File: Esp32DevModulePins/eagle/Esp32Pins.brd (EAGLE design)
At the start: 100 x 80 mm, 2 parts

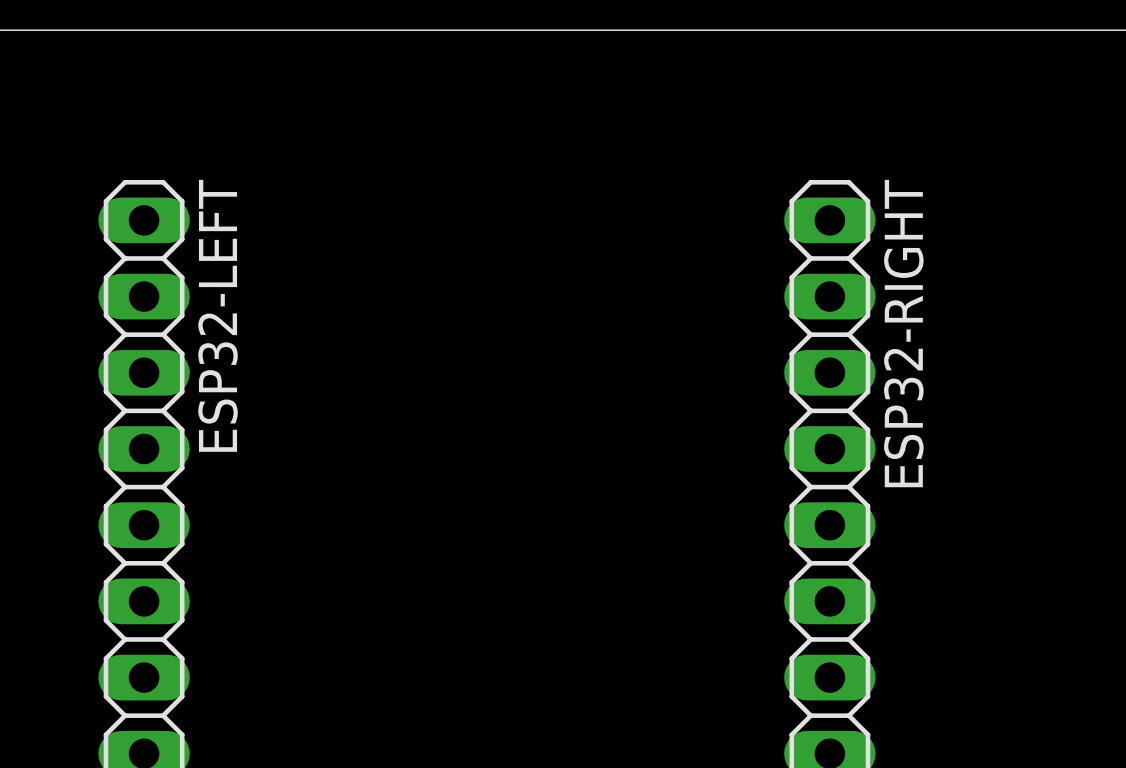
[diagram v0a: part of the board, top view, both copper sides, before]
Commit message: Corrected left vs right nomenclature
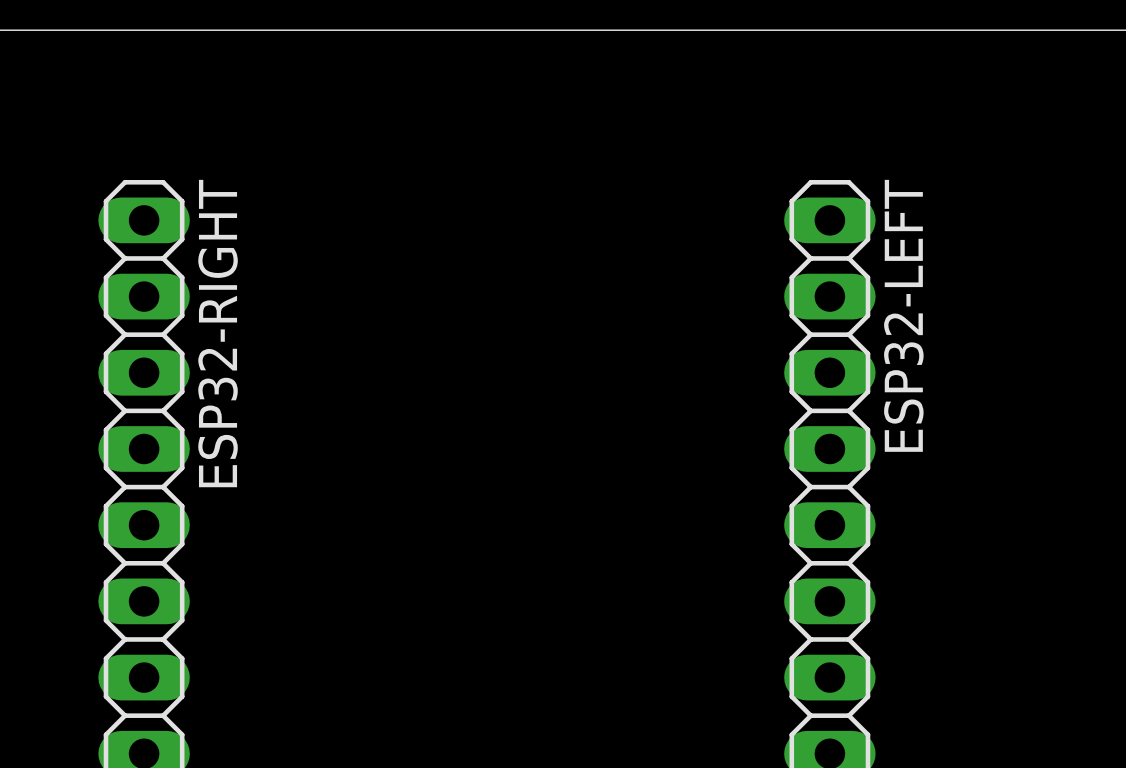
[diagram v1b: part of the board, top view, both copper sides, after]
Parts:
- moved ESP32-LEFT 22.9 mm to (29.2, 55.9)
- moved ESP32-RIGHT 22.9 mm to (6.35, 55.9)
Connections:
- net 3V3: now also ESP32-RIGHT.1; no longer ESP32-LEFT.1
- net D12: now also ESP32-LEFT.4; no longer ESP32-RIGHT.4
- net D13: now also ESP32-LEFT.3; no longer ESP32-RIGHT.3
- net D14: now also ESP32-LEFT.5; no longer ESP32-RIGHT.5
- net D15: now also ESP32-RIGHT.3; no longer ESP32-LEFT.3
- net D16: now also ESP32-RIGHT.6; no longer ESP32-LEFT.6
- net D17: now also ESP32-RIGHT.7; no longer ESP32-LEFT.7
- net D18: now also ESP32-RIGHT.9; no longer ESP32-LEFT.9
- net D19: now also ESP32-RIGHT.10; no longer ESP32-LEFT.10
- net D1_TX: now also ESP32-RIGHT.13; no longer ESP32-LEFT.13
- net D2: now also ESP32-RIGHT.4; no longer ESP32-LEFT.4
- net D21: now also ESP32-RIGHT.11; no longer ESP32-LEFT.11
- net D22: now also ESP32-RIGHT.14; no longer ESP32-LEFT.14
- net D23: now also ESP32-RIGHT.15; no longer ESP32-LEFT.15
- net D25: now also ESP32-LEFT.8; no longer ESP32-RIGHT.8
- net D26: now also ESP32-LEFT.7; no longer ESP32-RIGHT.7
- net D27: now also ESP32-LEFT.6; no longer ESP32-RIGHT.6
- net D32: now also ESP32-LEFT.10; no longer ESP32-RIGHT.10
- net D33: now also ESP32-LEFT.9; no longer ESP32-RIGHT.9
- net D3_RX: now also ESP32-RIGHT.12; no longer ESP32-LEFT.12
- net D4: now also ESP32-RIGHT.5; no longer ESP32-LEFT.5
- net D5: now also ESP32-RIGHT.8; no longer ESP32-LEFT.8
- net I34: now also ESP32-LEFT.12; no longer ESP32-RIGHT.12
- net I35: now also ESP32-LEFT.11; no longer ESP32-RIGHT.11
- net I36: now also ESP32-LEFT.14; no longer ESP32-RIGHT.14
- net I39: now also ESP32-LEFT.13; no longer ESP32-RIGHT.13
- net RESET: now also ESP32-LEFT.15; no longer ESP32-RIGHT.15
- net VIN: now also ESP32-LEFT.1; no longer ESP32-RIGHT.1
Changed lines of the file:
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@@
 <?xml version="1.0" encoding="utf-8"?>
 <!DOCTYPE eagle SYSTEM "eagle.dtd">
-<eagle version="9.5.2">
+<eagle version="9.6.2">
 <drawing>
 <settings>
@@
 </autorouter>
 <elements>
-<element name="ESP32-LEFT" library="pinhead" library_urn="urn:adsk.eagle:library:325" package="1X15" package3d_urn="urn:adsk.eagle:package:22424/2" value="0" x="6.35" y="55.88" smashed="yes" rot="R270">
+<element name="ESP32-RIGHT" library="pinhead" library_urn="urn:adsk.eagle:library:325" package="1X15" package3d_urn="urn:adsk.eagle:package:22424/2" value="0" x="6.35" y="55.88" smashed="yes" rot="R270">
 <attribute name="NAME" x="8.1788" y="75.0062" size="1.27" layer="25" ratio="10" rot="R270"/>
 <attribute name="POPULARITY" value="4" x="6.35" y="55.88" size="1.778" layer="27" rot="R270" display="off"/>
 </element>
-<element name="ESP32-RIGHT" library="pinhead" library_urn="urn:adsk.eagle:library:325" package="1X15" package3d_urn="urn:adsk.eagle:package:22424/2" value="0" x="29.21" y="55.88" smashed="yes" rot="R270">
+<element name="ESP32-LEFT" library="pinhead" library_urn="urn:adsk.eagle:library:325" package="1X15" package3d_urn="urn:adsk.eagle:package:22424/2" value="0" x="29.21" y="55.88" smashed="yes" rot="R270">
 <attribute name="NAME" x="31.0388" y="75.0062" size="1.27" layer="25" ratio="10" rot="R270"/>
 <attribute name="POPULARITY" value="4" x="29.21" y="55.88" size="1.778" layer="27" rot="R270" display="off"/>
@@
 <signals>
 <signal name="VIN">
+<contactref element="ESP32-LEFT" pad="1"/>
+</signal>
+<signal name="GND">
+<contactref element="ESP32-RIGHT" pad="2"/>
+<contactref element="ESP32-LEFT" pad="2"/>
+<wire x1="29.21" y1="71.12" x2="6.35" y2="71.12" width="0" layer="19" extent="1-1"/>
+</signal>
+<signal name="D13">
+<contactref element="ESP32-LEFT" pad="3"/>
+</signal>
+<signal name="D12">
+<contactref element="ESP32-LEFT" pad="4"/>
+</signal>
+<signal name="D27">
+<contactref element="ESP32-LEFT" pad="6"/>
+</signal>
+<signal name="D26">
+<contactref element="ESP32-LEFT" pad="7"/>
+</signal>
+<signal name="D25">
+<contactref element="ESP32-LEFT" pad="8"/>
+</signal>
+<signal name="D33">
+<contactref element="ESP32-LEFT" pad="9"/>
+</signal>
+<signal name="D32">
+<contactref element="ESP32-LEFT" pad="10"/>
+</signal>
+<signal name="I35">
+<contactref element="ESP32-LEFT" pad="11"/>
+</signal>
+<signal name="I36">
+<contactref element="ESP32-LEFT" pad="14"/>
+</signal>
+<signal name="RESET">
+<contactref element="ESP32-LEFT" pad="15"/>
+</signal>
+<signal name="D14">
+<contactref element="ESP32-LEFT" pad="5"/>
+</signal>
+<signal name="I39">
+<contactref element="ESP32-LEFT" pad="13"/>
+</signal>
+<signal name="I34">
+<contactref element="ESP32-LEFT" pad="12"/>
+</signal>
+<signal name="3V3">
 <contactref element="ESP32-RIGHT" pad="1"/>
 </signal>
-<signal name="GND">
-<contactref element="ESP32-LEFT" pad="2"/>
-<contactref element="ESP32-RIGHT" pad="2"/>
-<wire x1="29.21" y1="71.12" x2="6.35" y2="71.12" width="0" layer="19" extent="1-1"/>
-</signal>
-<signal name="D13">
+<signal name="D15">
 <contactref element="ESP32-RIGHT" pad="3"/>
 </signal>
-<signal name="D12">
+<signal name="D2">
 <contactref element="ESP32-RIGHT" pad="4"/>
 </signal>
-<signal name="D27">
+<signal name="D4">
+<contactref element="ESP32-RIGHT" pad="5"/>
+</signal>
+<signal name="D16">
 <contactref element="ESP32-RIGHT" pad="6"/>
 </signal>
-<signal name="D26">
+<signal name="D17">
 <contactref element="ESP32-RIGHT" pad="7"/>
 </signal>
-<signal name="D25">
+<signal name="D5">
 <contactref element="ESP32-RIGHT" pad="8"/>
 </signal>
-<signal name="D33">
+<signal name="D18">
 <contactref element="ESP32-RIGHT" pad="9"/>
 </signal>
-<signal name="D32">
+<signal name="D19">
 <contactref element="ESP32-RIGHT" pad="10"/>
 </signal>
-<signal name="I35">
+<signal name="D21">
 <contactref element="ESP32-RIGHT" pad="11"/>
 </signal>
-<signal name="I36">
+<signal name="D22">
 <contactref element="ESP32-RIGHT" pad="14"/>
 </signal>
-<signal name="RESET">
+<signal name="D23">
 <contactref element="ESP32-RIGHT" pad="15"/>
 </signal>
-<signal name="D14">
-<contactref element="ESP32-RIGHT" pad="5"/>
-</signal>
-<signal name="I39">
+<signal name="D3_RX">
+<contactref element="ESP32-RIGHT" pad="12"/>
+</signal>
+<signal name="D1_TX">
 <contactref element="ESP32-RIGHT" pad="13"/>
 </signal>
-<signal name="I34">
-<contactref element="ESP32-RIGHT" pad="12"/>
-</signal>
-<signal name="3V3">
-<contactref element="ESP32-LEFT" pad="1"/>
-</signal>
-<signal name="D15">
-<contactref element="ESP32-LEFT" pad="3"/>
-</signal>
-<signal name="D2">
-<contactref element="ESP32-LEFT" pad="4"/>
-</signal>
-<signal name="D4">
-<contactref element="ESP32-LEFT" pad="5"/>
-</signal>
-<signal name="D16">
-<contactref element="ESP32-LEFT" pad="6"/>
-</signal>
-<signal name="D17">
-<contactref element="ESP32-LEFT" pad="7"/>
-</signal>
-<signal name="D5">
-<contactref element="ESP32-LEFT" pad="8"/>
-</signal>
-<signal name="D18">
-<contactref element="ESP32-LEFT" pad="9"/>
-</signal>
-<signal name="D19">
-<contactref element="ESP32-LEFT" pad="10"/>
-</signal>
-<signal name="D21">
-<contactref element="ESP32-LEFT" pad="11"/>
-</signal>
-<signal name="D22">
-<contactref element="ESP32-LEFT" pad="14"/>
-</signal>
-<signal name="D23">
-<contactref element="ESP32-LEFT" pad="15"/>
-</signal>
-<signal name="D3_RX">
-<contactref element="ESP32-LEFT" pad="12"/>
-</signal>
-<signal name="D1_TX">
-<contactref element="ESP32-LEFT" pad="13"/>
-</signal>
 </signals>
